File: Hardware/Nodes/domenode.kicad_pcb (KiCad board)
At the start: 2 copper layers, 100 x 70 mm, 83 parts, among them J1 MIC_JUMPER, J10 5V, J11 TOUCH, J12 24V, J13 CAN_BOARD, J15 RGB_SHIELD, J16 RGB_SHIELD, J17 GROVE/I2C, J18 ISP, J19 CAN_IN, J2 MIC_HEADER, J20 CAN_OUT, J21 SWITCHES, J3 SW0, J4 CANTERM, J5 3V3, J6 POWER_TEST, J7 SPEAKER, J9 SENSOR, SW1 SW1, SW2 SW2, SW3 RESET, SW4 BOOT, U1 MINI-360, U2 AMS1117-3.3, U3 ESP32-WROOM, U5 TSDP341xx, U6 SN65HVD230

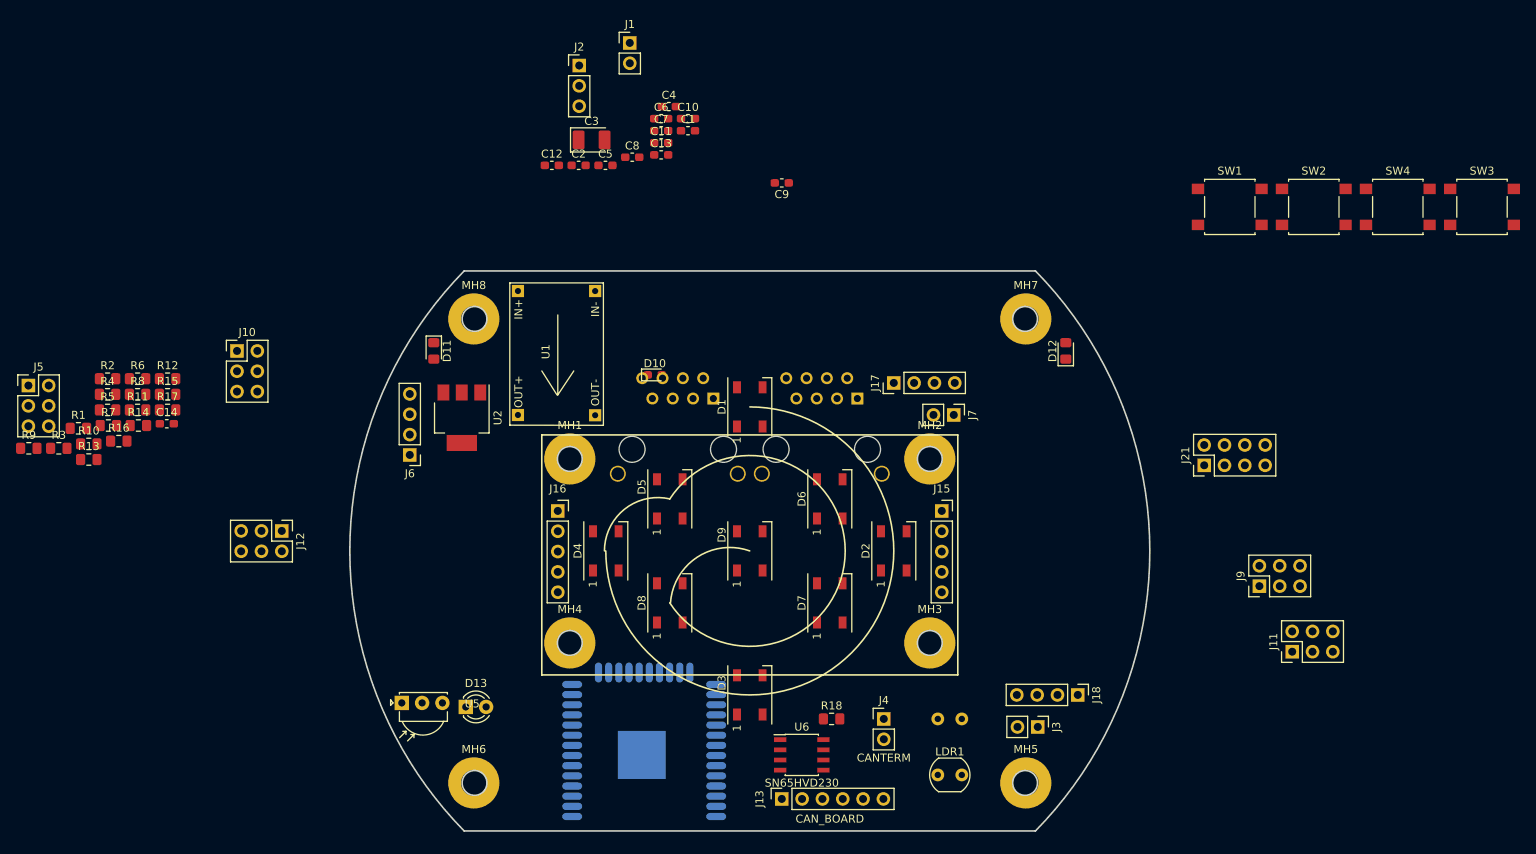
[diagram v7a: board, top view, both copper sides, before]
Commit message: Added cap for D9
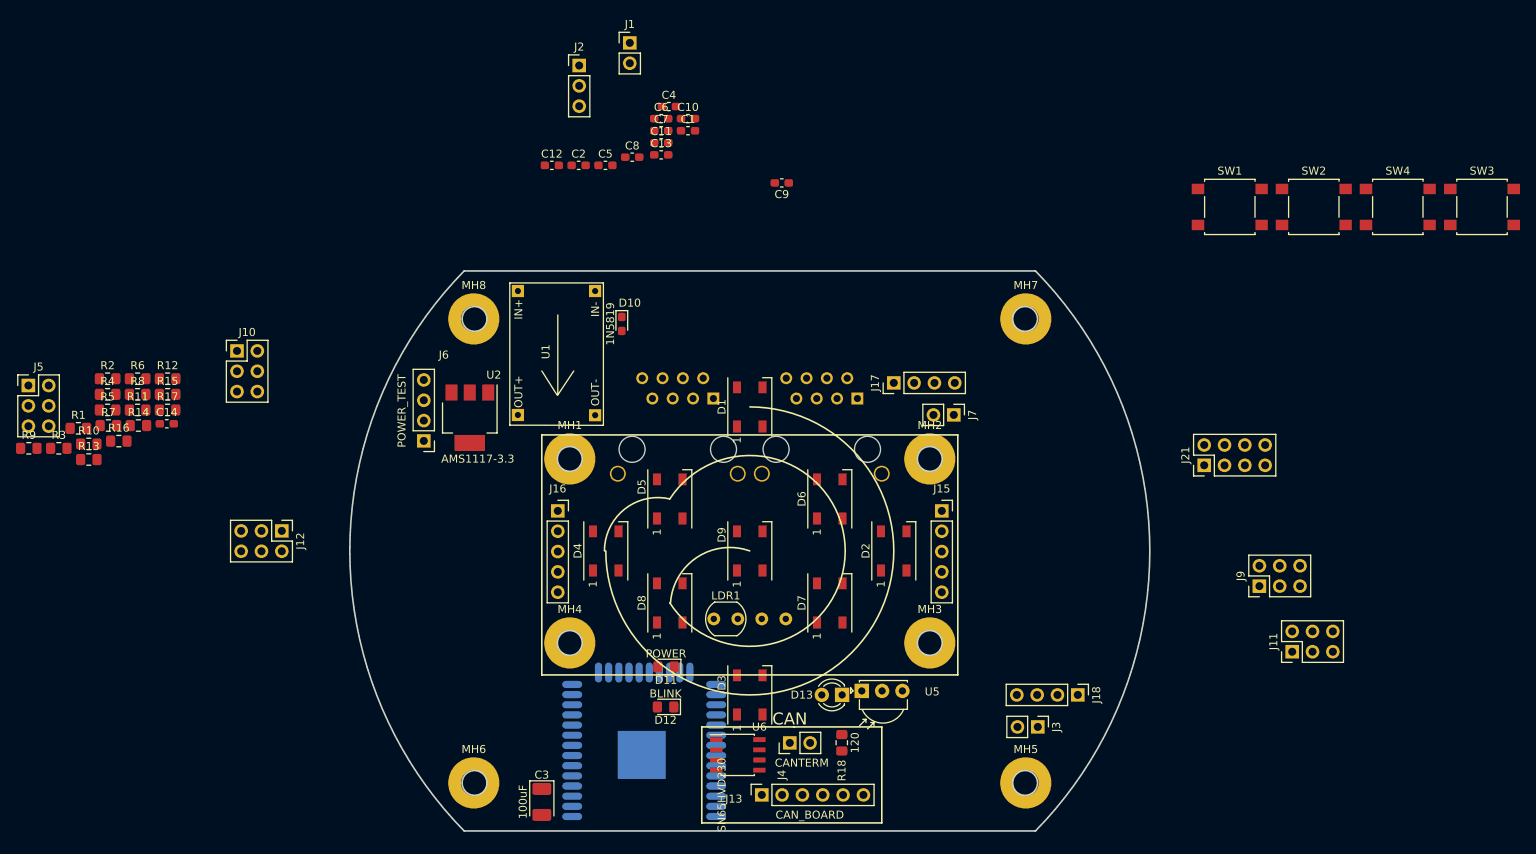
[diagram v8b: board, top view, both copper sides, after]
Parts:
- moved C3 83.0 mm to (122.5, 136.4), turned to 270 degrees
- moved D12 67.0 mm to (138.0, 124.5), turned to 180 degrees
- moved U5 57.5 mm to (162.5, 122.5)
- moved D11 49.0 mm to (138.0, 119.5), turned to 180 degrees
- moved D13 47.1 mm to (160.0, 123.0), turned to 180 degrees
- moved LDR1 34.1 mm to (144.0, 113.5)
- moved LDR2 25.3 mm to (150.0, 113.5)
- moved J4 12.1 mm to (153.5, 129.0), turned to 90 degrees
- moved U6 8.00 mm to (147.0, 130.5)
- moved D10 7.59 mm to (132.5, 76.6), turned to 270 degrees
- moved R18 3.24 mm to (160.0, 129.0), turned to 90 degrees
- moved J13 2.55 mm to (150.0, 135.5)
- moved J6 2.47 mm to (107.8, 91.2)
- moved U2 1.00 mm to (113.5, 88.3)
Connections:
- J6 pad 1: CANV -> CANGND
- J6 pad 2: +5V -> VCC
- J6 pad 3: VCC -> +5V
- J6 pad 4: CANGND -> CANV
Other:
- board text added: "CAN"
